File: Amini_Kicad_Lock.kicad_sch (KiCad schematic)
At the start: 47 parts, among them J1 Conn_01x02, J2 Conn_01x04, U1 nRF5340-QKxx, X1 ${ALTIUM_VALUE}, X2 ${ALTIUM_VALUE}

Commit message: 2. commit
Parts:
- removed C2: ${ALTIUM_VALUE}, CAPC0603X03L_C, symbol pca10143_sheet2_nrf5340_mcu-altium-import:root_1_CAP
- removed C3: ${ALTIUM_VALUE}, Capacitor_SMD:C_0201_0603Metric_Pad0.64x0.40mm_HandSolder, symbol pca10143_sheet2_nrf5340_mcu-altium-import:root_1_CAP
- removed L1: ${ALTIUM_VALUE}, INDC0603X03L_C, symbol pca10143_sheet2_nrf5340_mcu-altium-import:root_0_mirrored_IND
- removed TP10, TP9: TestPoint_Alt, TestPoint:TestPoint_Pad_1.5x1.5mm, symbol Connector:TestPoint_Alt
- removed TP13, TP15, TP6, TP7, TP8: TestPoint_Alt, TestPoint:TestPoint_THTPad_2.0x2.0mm_Drill1.0mm, symbol Connector:TestPoint_Alt
- added J3: MM8130-2600RA2, MM8130-2600RA2 antenna:MURATA_MM8130-2600RA2, symbol MM8130-2600RA2:MM8130-2600RA2
- C10: footprint CAPC0603X03L_C -> Inductor_SMD:L_0603_1608Metric
- C4: footprint CAPC0603X03L_C_NC -> Inductor_SMD:L_0603_1608Metric
- L3: footprint INDC0603X03L_C -> Inductor_SMD:L_0603_1608Metric
- TP1: footprint TestPoint:TestPoint_Pad_1.0x1.0mm -> TestPoint:TestPoint_Pad_D1.0mm
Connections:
- net GND: now also TP1.1, J3.GND1 (GND), J3.GND2 (GND), J3.GND3 (GND), J3.GND4 (GND)
- net at C4.2, L3.2: now also J3.IN; no longer TP1.1
- net at A1.1: now also J3.OUT
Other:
- moved on the sheet: A1

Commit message: 3. commit
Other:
- moved on the sheet: J2, TP1, TP11, TP12, TP14
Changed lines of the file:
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@@
 	)
 	(junction
-		(at 210.82 88.9)
+		(at 210.82 69.85)
 		(diameter 0)
 		(color 0 0 0 0)
@@
 	(wire
 		(pts
-			(xy 237.49 83.82) (xy 210.82 83.82)
+			(xy 237.49 64.77) (xy 210.82 64.77)
 		)
 		(stroke
@@
 	(wire
 		(pts
-			(xy 210.82 88.9) (xy 229.87 88.9)
+			(xy 210.82 69.85) (xy 229.87 69.85)
 		)
 		(stroke
@@
 	(wire
 		(pts
-			(xy 256.54 86.36) (xy 210.82 86.36)
+			(xy 256.54 67.31) (xy 210.82 67.31)
 		)
 		(stroke
@@
 	(wire
 		(pts
-			(xy 222.25 81.28) (xy 210.82 81.28)
+			(xy 222.25 62.23) (xy 210.82 62.23)
 		)
 		(stroke
@@
 	)
 	(label "SWDIO"
-		(at 212.09 83.82 0)
+		(at 212.09 64.77 0)
 		(fields_autoplaced yes)
 		(effects
@@
 	)
 	(label "SWDCLK"
-		(at 212.09 81.28 0)
+		(at 212.09 62.23 0)
 		(fields_autoplaced yes)
 		(effects
@@
 	)
 	(label "~{RESET}"
-		(at 212.09 86.36 0)
+		(at 212.09 67.31 0)
 		(fields_autoplaced yes)
 		(effects
@@
 	(symbol
 		(lib_id "nrf5340_qkaa_config3-altium-import:GND_POWER_GROUND")
-		(at 210.82 88.9 0)
+		(at 210.82 69.85 0)
 		(unit 1)
 		(exclude_from_sim no)
@@
 		(dnp no)
 		(property "Reference" "#PWR021"
-			(at 210.82 88.9 0)
+			(at 210.82 69.85 0)
 			(effects
 				(font
@@
 		)
 		(property "Value" "GND"
-			(at 210.82 95.25 0)
+			(at 210.82 76.2 0)
 			(effects
 				(font
@@
 		)
 		(property "Footprint" ""
-			(at 210.82 88.9 0)
+			(at 210.82 69.85 0)
 			(effects
 				(font
@@
 		)
 		(property "Datasheet" ""
-			(at 210.82 88.9 0)
+			(at 210.82 69.85 0)
 			(effects
 				(font
@@
 		)
 		(property "Description" ""
-			(at 210.82 88.9 0)
+			(at 210.82 69.85 0)
 			(effects
 				(font
@@
 	(symbol
 		(lib_id "Connector:TestPoint")
-		(at 256.54 86.36 270)
+		(at 256.54 67.31 270)
 		(unit 1)
 		(exclude_from_sim no)
@@
 		(fields_autoplaced yes)
 		(property "Reference" "TP14"
-			(at 261.62 85.0899 90)
+			(at 261.62 66.0399 90)
 			(effects
 				(font
@@
 		)
 		(property "Value" "TestPoint"
-			(at 261.62 87.6299 90)
+			(at 261.62 68.5799 90)
 			(effects
 				(font
@@
 		)
 		(property "Footprint" "TestPoint:TestPoint_Pad_D1.0mm"
-			(at 256.54 91.44 0)
+			(at 256.54 72.39 0)
 			(effects
 				(font
@@
 		)
 		(property "Datasheet" "~"
-			(at 256.54 91.44 0)
+			(at 256.54 72.39 0)
 			(effects
 				(font
@@
 		)
 		(property "Description" "test point"
-			(at 256.54 86.36 0)
+			(at 256.54 67.31 0)
 			(effects
 				(font
@@
 	(symbol
 		(lib_id "Connector:TestPoint")
-		(at 237.49 83.82 270)
+		(at 237.49 64.77 270)
 		(unit 1)
 		(exclude_from_sim no)
@@
 		(fields_autoplaced yes)
 		(property "Reference" "TP12"
-			(at 242.57 82.5499 90)
+			(at 242.57 63.4999 90)
 			(effects
 				(font
@@
 		)
 		(property "Value" "TestPoint"
-			(at 242.57 85.0899 90)
+			(at 242.57 66.0399 90)
 			(effects
 				(font
@@
 		)
 		(property "Footprint" "TestPoint:TestPoint_Pad_D1.0mm"
-			(at 237.49 88.9 0)
+			(at 237.49 69.85 0)
 			(effects
 				(font
@@
 		)
 		(property "Datasheet" "~"
-			(at 237.49 88.9 0)
+			(at 237.49 69.85 0)
 			(effects
 				(font
@@
 		)
 		(property "Description" "test point"
-			(at 237.49 83.82 0)
+			(at 237.49 64.77 0)
 			(effects
 				(font
@@
 	(symbol
 		(lib_id "Connector_Generic:Conn_01x04")
-		(at 205.74 86.36 180)
+		(at 205.74 67.31 180)
 		(unit 1)
 		(exclude_from_sim no)
@@
 		(dnp no)
 		(property "Reference" "J2"
-			(at 205.74 74.93 0)
+			(at 205.74 55.88 0)
 			(effects
 				(font
@@
 		)
 		(property "Value" "Conn_01x04"
-			(at 205.74 77.47 0)
+			(at 205.74 58.42 0)
 			(effects
 				(font
@@
 		)
 		(property "Footprint" "Connector_JST:JST_SH_SM04B-SRSS-TB_1x04-1MP_P1.00mm_Horizontal"
-			(at 205.74 86.36 0)
+			(at 205.74 67.31 0)
 			(effects
 				(font
@@
 		)
 		(property "Datasheet" "~"
-			(at 205.74 86.36 0)
+			(at 205.74 67.31 0)
 			(effects
 				(font
@@
 		)
 		(property "Description" "Generic connector, single row, 01x04, script generated (kicad-library-utils/schlib/autogen/connector/)"
-			(at 205.74 86.36 0)
+			(at 205.74 67.31 0)
 			(effects
 				(font
@@
 	(symbol
 		(lib_id "Connector:TestPoint")
-		(at 222.25 81.28 270)
+		(at 222.25 62.23 270)
 		(unit 1)
 		(exclude_from_sim no)
@@
 		(fields_autoplaced yes)
 		(property "Reference" "TP11"
-			(at 227.33 80.0099 90)
+			(at 227.33 60.9599 90)
 			(effects
 				(font
@@
 		)
 		(property "Value" "TestPoint"
-			(at 227.33 82.5499 90)
+			(at 227.33 63.4999 90)
 			(effects
 				(font
@@
 		)
 		(property "Footprint" "TestPoint:TestPoint_Pad_D1.0mm"
-			(at 222.25 86.36 0)
+			(at 222.25 67.31 0)
 			(effects
 				(font
@@
 		)
 		(property "Datasheet" "~"
-			(at 222.25 86.36 0)
+			(at 222.25 67.31 0)
 			(effects
 				(font
@@
 		)
 		(property "Description" "test point"
-			(at 222.25 81.28 0)
+			(at 222.25 62.23 0)
 			(effects
 				(font
@@
 	(symbol
 		(lib_id "Connector:TestPoint")
-		(at 229.87 88.9 270)
+		(at 229.87 69.85 270)
 		(unit 1)
 		(exclude_from_sim no)
@@
 		(fields_autoplaced yes)
 		(property "Reference" "TP1"
-			(at 234.95 87.6299 90)
+			(at 234.95 68.5799 90)
 			(effects
 				(font
@@
 		)
 		(property "Value" "TestPoint"
-			(at 234.95 90.1699 90)
+			(at 234.95 71.1199 90)
 			(effects
 				(font
@@
 		)
 		(property "Footprint" "TestPoint:TestPoint_Pad_D1.0mm"
-			(at 229.87 93.98 0)
+			(at 229.87 74.93 0)
 			(effects
 				(font
@@
 		)
 		(property "Datasheet" "~"
-			(at 229.87 93.98 0)
+			(at 229.87 74.93 0)
 			(effects
 				(font
@@
 		)
 		(property "Description" "test point"
-			(at 229.87 88.9 0)
+			(at 229.87 69.85 0)
 			(effects
 				(font

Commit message: clear, every component on place, wrong with shematic
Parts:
- renumbered C10 to C1, C12 to C10, C16 to C11, C13 to C12, C17 to C13, C18 to C15, C19 to C16, C4 to C18, C1 to C2, C5 to C3, C7 to C4, C8 to C5, C9 to C7, C11 to C8, C15 to C9, L3 to L1, L4 to L3, TP11 to TP3, TP12 to TP4, TP14 to TP5
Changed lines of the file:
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@@
 		(on_board yes)
 		(dnp no)
-		(property "Reference" "C10"
+		(property "Reference" "C1"
 			(at 72.898 138.43 0)
 			(effects
@@
 			(project "Amini_Kicad_Lock"
 				(path "/030762cc-f5a7-43ca-9be6-07123a61669e"
-					(reference "C10")
+					(reference "C1")
 					(unit 1)
 				)
@@
 		(on_board yes)
 		(dnp no)
-		(property "Reference" "C19"
+		(property "Reference" "C16"
 			(at 267.462 20.32 0)
 			(effects
@@
 			(project "Amini_Kicad_Lock"
 				(path "/030762cc-f5a7-43ca-9be6-07123a61669e"
-					(reference "C19")
+					(reference "C16")
 					(unit 1)
 				)
@@
 		(on_board yes)
 		(dnp no)
-		(property "Reference" "C17"
+		(property "Reference" "C13"
 			(at 245.872 20.32 0)
 			(effects
@@
 			(project "Amini_Kicad_Lock"
 				(path "/030762cc-f5a7-43ca-9be6-07123a61669e"
-					(reference "C17")
+					(reference "C13")
 					(unit 1)
 				)
@@
 		(on_board yes)
 		(dnp no)
-		(property "Reference" "C12"
+		(property "Reference" "C10"
 			(at 195.072 20.32 0)
 			(effects
@@
 			(project "Amini_Kicad_Lock"
 				(path "/030762cc-f5a7-43ca-9be6-07123a61669e"
-					(reference "C12")
+					(reference "C10")
 					(unit 1)
 				)
@@
 		(dnp no)
 		(fields_autoplaced yes)
-		(property "Reference" "TP14"
+		(property "Reference" "TP5"
 			(at 261.62 66.0399 90)
 			(effects
@@
 			(project "Amini_Kicad_Lock"
 				(path "/030762cc-f5a7-43ca-9be6-07123a61669e"
-					(reference "TP14")
+					(reference "TP5")
 					(unit 1)
 				)
@@
 		(dnp no)
 		(fields_autoplaced yes)
-		(property "Reference" "TP12"
+		(property "Reference" "TP4"
 			(at 242.57 63.4999 90)
 			(effects
@@
 			(project "Amini_Kicad_Lock"
 				(path "/030762cc-f5a7-43ca-9be6-07123a61669e"
-					(reference "TP12")
+					(reference "TP4")
 					(unit 1)
 				)
@@
 		(on_board yes)
 		(dnp no)
-		(property "Reference" "C4"
+		(property "Reference" "C18"
 			(at 46.482 138.43 0)
 			(effects
@@
 			(project "Amini_Kicad_Lock"
 				(path "/030762cc-f5a7-43ca-9be6-07123a61669e"
-					(reference "C4")
+					(reference "C18")
 					(unit 1)
 				)
@@
 		(on_board yes)
 		(dnp no)
-		(property "Reference" "C16"
+		(property "Reference" "C11"
 			(at 235.712 20.32 0)
 			(effects
@@
 			(project "Amini_Kicad_Lock"
 				(path "/030762cc-f5a7-43ca-9be6-07123a61669e"
-					(reference "C16")
+					(reference "C11")
 					(unit 1)
 				)
@@
 		(on_board yes)
 		(dnp no)
-		(property "Reference" "C1"
+		(property "Reference" "C2"
 			(at 22.352 33.02 0)
 			(effects
@@
 			(project "Amini_Kicad_Lock"
 				(path "/030762cc-f5a7-43ca-9be6-07123a61669e"
-					(reference "C1")
+					(reference "C2")
 					(unit 1)
 				)
@@
 		(on_board yes)
 		(dnp no)
-		(property "Reference" "C9"
+		(property "Reference" "C7"
 			(at 73.152 161.29 0)
 			(effects
@@
 			(project "Amini_Kicad_Lock"
 				(path "/030762cc-f5a7-43ca-9be6-07123a61669e"
-					(reference "C9")
+					(reference "C7")
 					(unit 1)
 				)
@@
 		(on_board yes)
 		(dnp no)
-		(property "Reference" "C7"
+		(property "Reference" "C4"
 			(at 73.152 92.71 0)
 			(effects
@@
 			(project "Amini_Kicad_Lock"
 				(path "/030762cc-f5a7-43ca-9be6-07123a61669e"
-					(reference "C7")
+					(reference "C4")
 					(unit 1)
 				)
@@
 		(on_board yes)
 		(dnp no)
-		(property "Reference" "C5"
+		(property "Reference" "C3"
 			(at 52.832 92.71 0)
 			(effects
@@
 			(project "Amini_Kicad_Lock"
 				(path "/030762cc-f5a7-43ca-9be6-07123a61669e"
-					(reference "C5")
+					(reference "C3")
 					(unit 1)
 				)
@@
 		(dnp no)
 		(fields_autoplaced yes)
-		(property "Reference" "TP11"
+		(property "Reference" "TP3"
 			(at 227.33 60.9599 90)
 			(effects
@@
 			(project "Amini_Kicad_Lock"
 				(path "/030762cc-f5a7-43ca-9be6-07123a61669e"
-					(reference "TP11")
+					(reference "TP3")
 					(unit 1)
 				)
@@
 		(on_board yes)
 		(dnp no)
-		(property "Reference" "C13"
+		(property "Reference" "C12"
 			(at 205.232 20.32 0)
 			(effects
@@
 			(project "Amini_Kicad_Lock"
 				(path "/030762cc-f5a7-43ca-9be6-07123a61669e"
-					(reference "C13")
+					(reference "C12")
 					(unit 1)
 				)
@@
 		(on_board yes)
 		(dnp no)
-		(property "Reference" "C15"
+		(property "Reference" "C9"
 			(at 225.552 20.32 0)
 			(effects
@@
 			(project "Amini_Kicad_Lock"
 				(path "/030762cc-f5a7-43ca-9be6-07123a61669e"
-					(reference "C15")
+					(reference "C9")
 					(unit 1)
 				)
@@
 		(on_board yes)
 		(dnp no)
-		(property "Reference" "C11"
+		(property "Reference" "C8"
 			(at 184.912 20.32 0)
 			(effects
@@
 			(project "Amini_Kicad_Lock"
 				(path "/030762cc-f5a7-43ca-9be6-07123a61669e"
-					(reference "C11")
+					(reference "C8")
 					(unit 1)
 				)
@@
 		(on_board yes)
 		(dnp no)
-		(property "Reference" "L3"
+		(property "Reference" "L1"
 			(at 66.548 132.588 0)
 			(effects
@@
 			(project "Amini_Kicad_Lock"
 				(path "/030762cc-f5a7-43ca-9be6-07123a61669e"
-					(reference "L3")
+					(reference "L1")
 					(unit 1)
 				)
@@
 		(on_board yes)
 		(dnp no)
-		(property "Reference" "L4"
+		(property "Reference" "L3"
 			(at 71.882 111.252 0)
 			(effects
@@
 			(project "Amini_Kicad_Lock"
 				(path "/030762cc-f5a7-43ca-9be6-07123a61669e"
-					(reference "L4")
+					(reference "L3")
 					(unit 1)
 				)
@@
 		(on_board yes)
 		(dnp no)
-		(property "Reference" "C18"
+		(property "Reference" "C15"
 			(at 256.032 20.32 0)
 			(effects
@@
 			(project "Amini_Kicad_Lock"
 				(path "/030762cc-f5a7-43ca-9be6-07123a61669e"
-					(reference "C18")
+					(reference "C15")
 					(unit 1)
 				)
@@
 		(on_board yes)
 		(dnp no)
-		(property "Reference" "C8"
+		(property "Reference" "C5"
 			(at 73.152 120.65 0)
 			(effects
@@
 			(project "Amini_Kicad_Lock"
 				(path "/030762cc-f5a7-43ca-9be6-07123a61669e"
-					(reference "C8")
+					(reference "C5")
 					(unit 1)
 				)

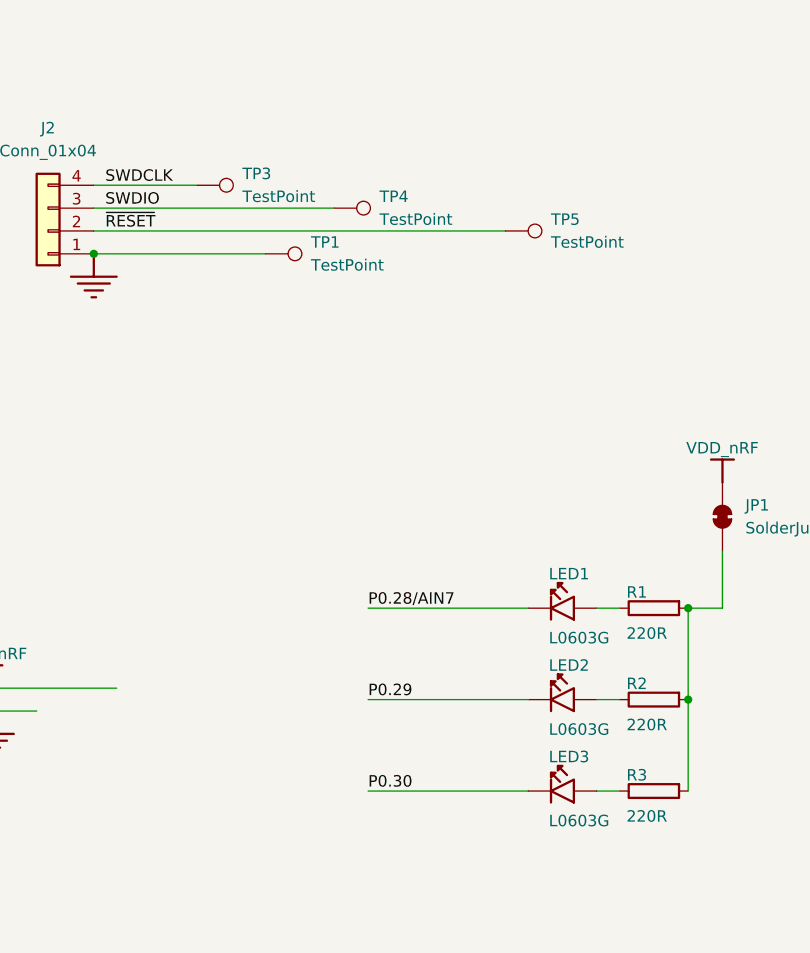
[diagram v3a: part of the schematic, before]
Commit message: mousebites added
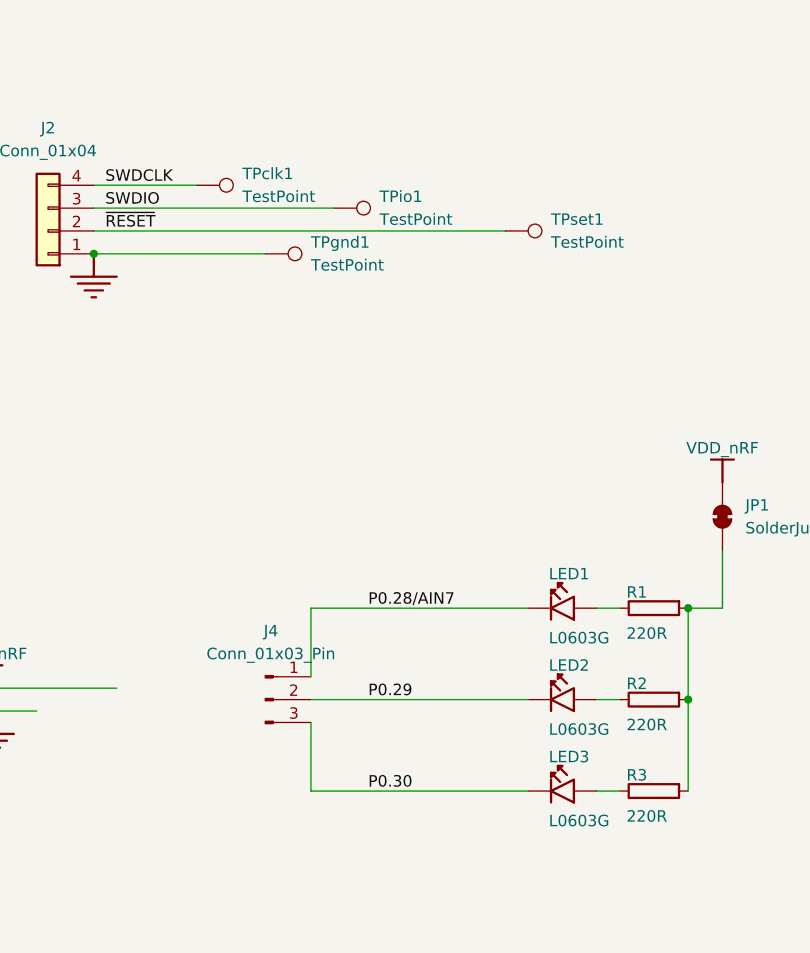
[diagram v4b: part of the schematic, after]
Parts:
- added J4: Conn_01x03_Pin, Connector_PinHeader_1.00mm:PinHeader_1x03_P1.00mm_Vertical, symbol Connector:Conn_01x03_Pin
- TPclk1: renamed from TP3; footprint TestPoint:TestPoint_Pad_D1.0mm -> TestPoint:TestPoint_Pad_D1.5mm
- TPgnd1: renamed from TP1; footprint TestPoint:TestPoint_Pad_D1.0mm -> TestPoint:TestPoint_Pad_D1.5mm
- TPio1: renamed from TP4; footprint TestPoint:TestPoint_Pad_D1.0mm -> TestPoint:TestPoint_Pad_D1.5mm
- TPset1: renamed from TP5; footprint TestPoint:TestPoint_Pad_D1.0mm -> TestPoint:TestPoint_Pad_D1.5mm
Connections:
- net P0.28/AIN7: now also J4.1 (Pin_1)
- net P0.29: now also J4.2 (Pin_2)
- net P0.30: now also J4.3 (Pin_3)
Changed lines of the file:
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@@
 	(wire
 		(pts
-			(xy 241.3 119.38) (xy 259.08 119.38)
-		)
-		(stroke
-			(width 0)
-			(type default)
-		)
-	)
-	(wire
-		(pts
 			(xy 78.74 74.93) (xy 50.8 74.93)
 		)
@@
 	(wire
 		(pts
-			(xy 241.3 109.22) (xy 259.08 109.22)
-		)
-		(stroke
-			(width 0)
-			(type default)
-		)
-	)
-	(wire
-		(pts
 			(xy 72.39 46.99) (xy 72.39 49.53)
 		)
@@
 	(wire
 		(pts
+			(xy 234.95 119.38) (xy 259.08 119.38)
+		)
+		(stroke
+			(width 0)
+			(type default)
+		)
+	)
+	(wire
+		(pts
 			(xy 210.82 69.85) (xy 229.87 69.85)
 		)
@@
 	(wire
 		(pts
+			(xy 234.95 109.22) (xy 234.95 116.84)
+		)
+		(stroke
+			(width 0)
+			(type default)
+		)
+	)
+	(wire
+		(pts
 			(xy 50.8 85.09) (xy 50.8 87.63)
 		)
@@
 	(wire
 		(pts
+			(xy 234.95 121.92) (xy 234.95 129.54)
+		)
+		(stroke
+			(width 0)
+			(type default)
+		)
+	)
+	(wire
+		(pts
 			(xy 78.74 24.13) (xy 67.31 24.13)
 		)
@@
 	(wire
 		(pts
+			(xy 234.95 109.22) (xy 259.08 109.22)
+		)
+		(stroke
+			(width 0)
+			(type default)
+		)
+	)
+	(wire
+		(pts
 			(xy 78.74 87.63) (xy 71.12 87.63)
 		)
@@
 	(wire
 		(pts
-			(xy 71.12 85.09) (xy 50.8 85.09)
+			(xy 234.95 129.54) (xy 259.08 129.54)
 		)
 		(stroke
@@
 	(wire
 		(pts
-			(xy 20.32 133.35) (xy 44.45 133.35)
+			(xy 71.12 85.09) (xy 50.8 85.09)
 		)
 		(stroke
@@
 	(wire
 		(pts
-			(xy 106.68 15.24) (xy 20.32 15.24)
+			(xy 20.32 133.35) (xy 44.45 133.35)
 		)
 		(stroke
@@
 	(wire
 		(pts
-			(xy 16.51 189.23) (xy 21.59 189.23)
+			(xy 106.68 15.24) (xy 20.32 15.24)
 		)
 		(stroke
@@
 	(wire
 		(pts
-			(xy 67.31 133.35) (xy 74.93 133.35)
+			(xy 16.51 189.23) (xy 21.59 189.23)
 		)
 		(stroke
@@
 	(wire
 		(pts
-			(xy 241.3 129.54) (xy 259.08 129.54)
+			(xy 67.31 133.35) (xy 74.93 133.35)
 		)
 		(stroke
@@
 		(dnp no)
 		(fields_autoplaced yes)
-		(property "Reference" "TP5"
+		(property "Reference" "TPset1"
 			(at 261.62 66.0399 90)
 			(effects
@@
 			)
 		)
-		(property "Footprint" "TestPoint:TestPoint_Pad_D1.0mm"
+		(property "Footprint" "TestPoint:TestPoint_Pad_D1.5mm"
 			(at 256.54 72.39 0)
 			(effects
@@
 			(project "Amini_Kicad_Lock"
 				(path "/030762cc-f5a7-43ca-9be6-07123a61669e"
-					(reference "TP5")
+					(reference "TPset1")
 					(unit 1)
 				)
@@
 		(dnp no)
 		(fields_autoplaced yes)
-		(property "Reference" "TP4"
+		(property "Reference" "TPio1"
 			(at 242.57 63.4999 90)
 			(effects
@@
 			)
 		)
-		(property "Footprint" "TestPoint:TestPoint_Pad_D1.0mm"
+		(property "Footprint" "TestPoint:TestPoint_Pad_D1.5mm"
 			(at 237.49 69.85 0)
 			(effects
@@
 			(project "Amini_Kicad_Lock"
 				(path "/030762cc-f5a7-43ca-9be6-07123a61669e"
-					(reference "TP4")
+					(reference "TPio1")
 					(unit 1)
 				)
@@
 	)
 	(symbol
+		(lib_id "Connector:Conn_01x03_Pin")
+		(at 229.87 119.38 0)
+		(unit 1)
+		(exclude_from_sim no)
+		(in_bom yes)
+		(on_board yes)
+		(dnp no)
+		(fields_autoplaced yes)
+		(property "Reference" "J4"
+			(at 230.505 111.76 0)
+			(effects
+				(font
+					(size 1.27 1.27)
+				)
+			)
+		)
+		(property "Value" "Conn_01x03_Pin"
+			(at 230.505 114.3 0)
+			(effects
+				(font
+					(size 1.27 1.27)
+				)
+			)
+		)
+		(property "Footprint" "Connector_PinHeader_1.00mm:PinHeader_1x03_P1.00mm_Vertical"
+			(at 229.87 119.38 0)
+			(effects
+				(font
+					(size 1.27 1.27)
+				)
+				(hide yes)
+			)
+		)
+		(property "Datasheet" "~"
+			(at 229.87 119.38 0)
+			(effects
+				(font
+					(size 1.27 1.27)
+				)
+				(hide yes)
+			)
+		)
+		(property "Description" "Generic connector, single row, 01x03, script generated"
+			(at 229.87 119.38 0)
+			(effects
+				(font
+					(size 1.27 1.27)
+				)
+				(hide yes)
+			)
+		)
+		(pin "3"
+		)
+		(pin "2"
+		)
+		(pin "1"
+		)
+		(instances
+			(project "Amini_Kicad_Lock"
+				(path "/030762cc-f5a7-43ca-9be6-07123a61669e"
+					(reference "J4")
+					(unit 1)
+				)
+			)
+		)
+	)
+	(symbol
 		(lib_id "nrf5340_qkaa_config3-altium-import:root_3_CAP")
 		(at 233.68 15.24 0)
@@
 		(dnp no)
 		(fields_autoplaced yes)
-		(property "Reference" "TP3"
+		(property "Reference" "TPclk1"
 			(at 227.33 60.9599 90)
 			(effects
@@
 			)
 		)
-		(property "Footprint" "TestPoint:TestPoint_Pad_D1.0mm"
+		(property "Footprint" "TestPoint:TestPoint_Pad_D1.5mm"
 			(at 222.25 67.31 0)
 			(effects
@@
 			(project "Amini_Kicad_Lock"
 				(path "/030762cc-f5a7-43ca-9be6-07123a61669e"
-					(reference "TP3")
+					(reference "TPclk1")
 					(unit 1)
 				)
@@
 		(dnp no)
 		(fields_autoplaced yes)
-		(property "Reference" "TP1"
+		(property "Reference" "TPgnd1"
 			(at 234.95 68.5799 90)
 			(effects
@@
 			)
 		)
-		(property "Footprint" "TestPoint:TestPoint_Pad_D1.0mm"
+		(property "Footprint" "TestPoint:TestPoint_Pad_D1.5mm"
 			(at 229.87 74.93 0)
 			(effects
@@
 			(project "Amini_Kicad_Lock"
 				(path "/030762cc-f5a7-43ca-9be6-07123a61669e"
-					(reference "TP1")
+					(reference "TPgnd1")
 					(unit 1)
 				)
